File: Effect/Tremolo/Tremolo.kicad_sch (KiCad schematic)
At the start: 28 parts, among them J1 Conn_01x04_Pin, J2 Conn_01x03_Pin, Q1 MBT2222ADW1T1, Q2 MMBF5103, Q3 BC846

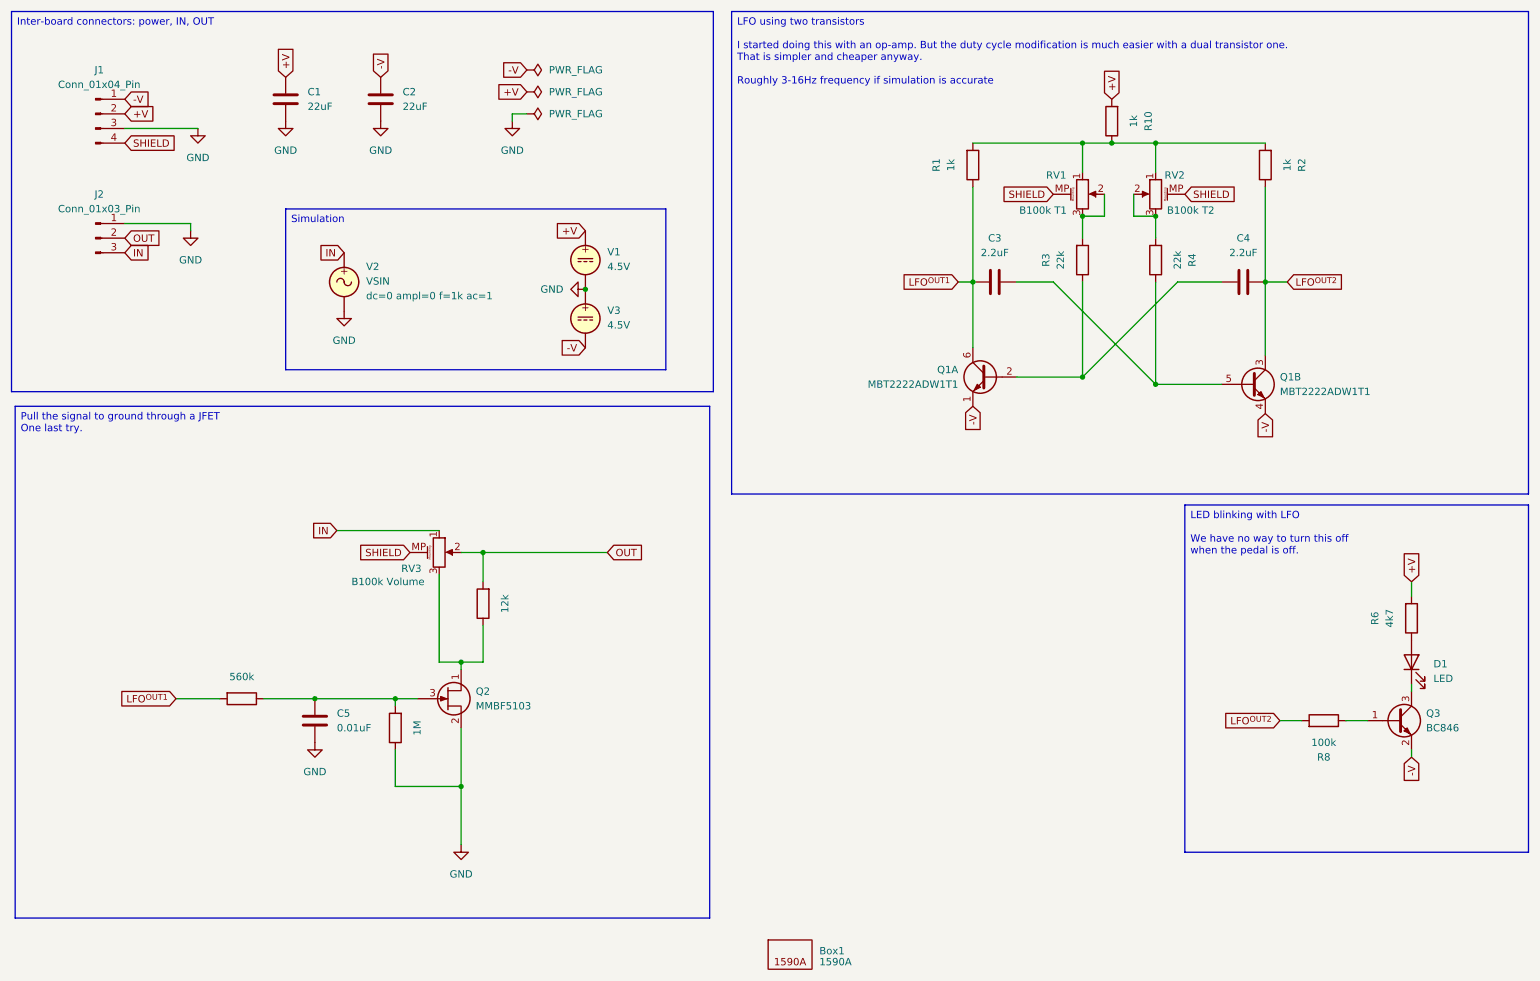
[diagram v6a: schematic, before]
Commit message: Start converting effects boards to the 5V base board: tremolo
The original effects boards were designed to not actually care too much
about the details of the voltage rail, but that was never true of the
tremolo board - because the transistor V_{GS(off)} voltage matters.

Yet the tremolo board was made to _look_ like it didn't care about the
details of the rails, having the non-specific +V and -V rails, and
calling the signal ground reference "GND".

That signal ground vs power ground thing obviously then caused the
additional issue with the schematic using the signal voltage reference
as a power rail for the LFO, fixed in commit 63201d9 ("Quick dirty fix
for tremolo board").

The digital effects boards already made their voltage rails explicit,
and match the base board they require.  Let's just start doing that with
the other effects boards too, starting with the tremolo that cares the
most.

Since I have to start using the 5V rail-to-rail op amps anyway, and I
don't want to have lots of component variations for different boards, I
think I'm going to convert them all to the new world order.

And while 9V may be traditional, a lot of modern components seem to all
be geared to 5V or less.  Of course, there are also op amps like the
OPAx991 family that have very wide voltage rails indeed, and are RtR
from 2.7V to 40V rails.  But with other components having much more
limited voltage ranges, I don't think it's worth designing different
base boards.

For the tremolo board, the only real change for 5V involves removing the
voltage divider resistor that was part of driving the JFET.  With the 9V
voltage rails, that just intentionally limited the gate voltage swing.

Now, with the 5V rails, it ended up limiting the gate voltage too much,
and the JFET might not turn on at all depending on exactly where
V_{GS(off)} ends up being.

And since we're now being honest about what is real ground, just make
the shield be GND and use a full ground pour.

Signed-off-by: Linus Torvalds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
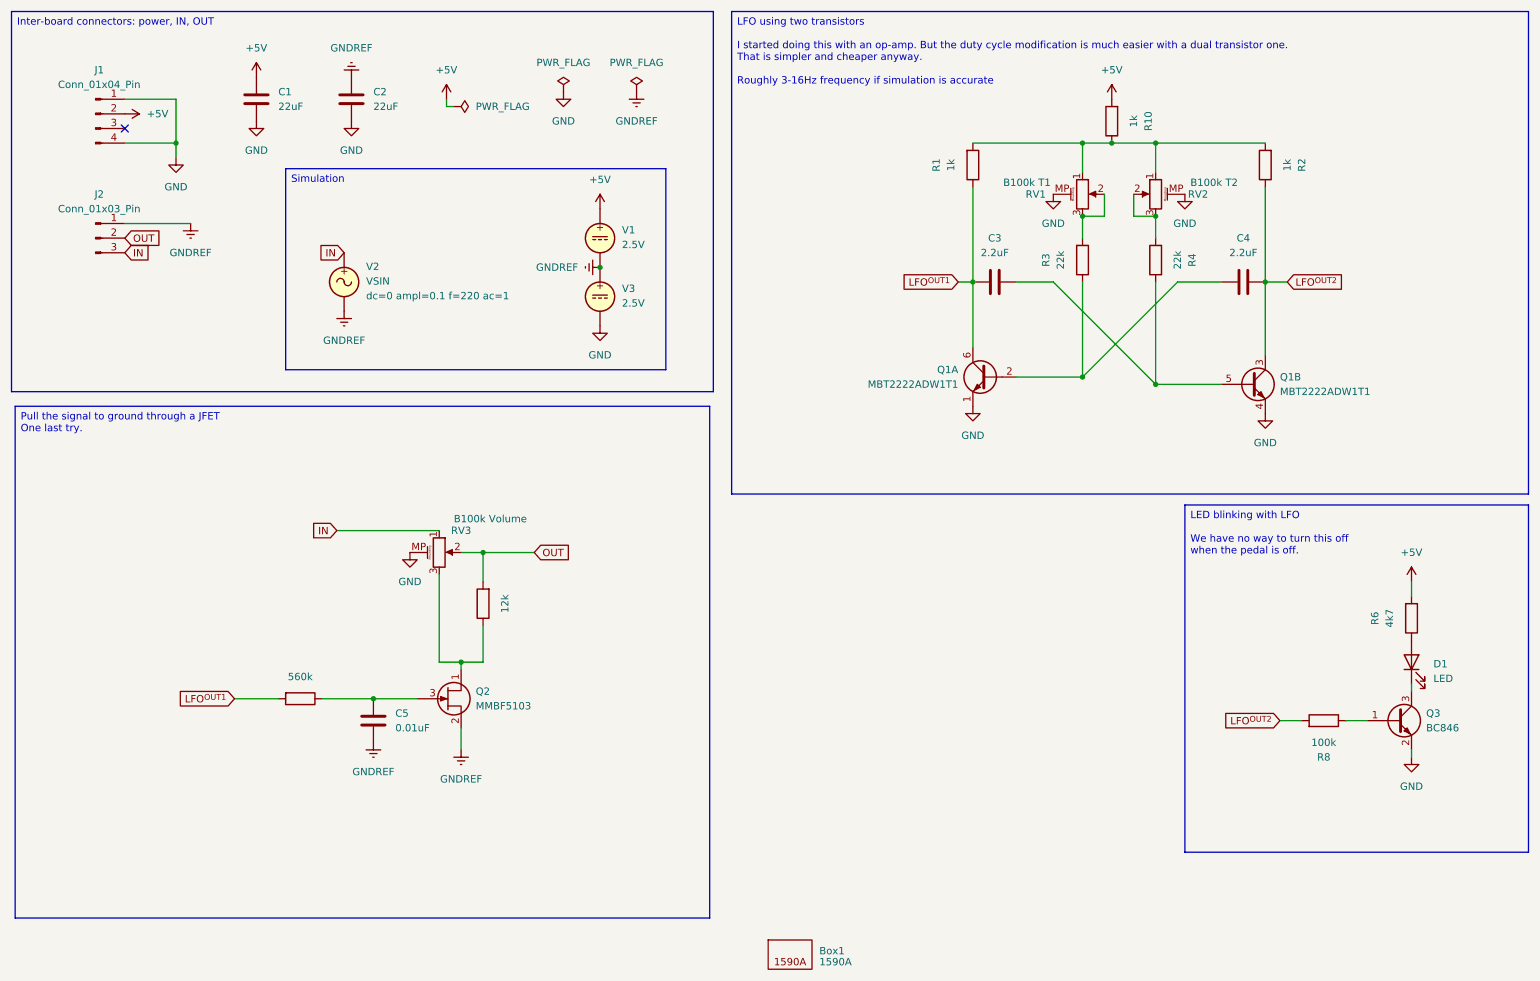
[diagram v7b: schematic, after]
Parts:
- removed R9: 1M, Resistor_SMD:R_0805_2012Metric_Pad1.20x1.40mm_HandSolder, symbol Device:R
- V1, V3: value 4.5V -> 2.5V
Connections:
- net SHIELD is gone; now on net GND: J1.4 (Pin_4), RV1.MP (MountPin), RV2.MP (MountPin), RV3.MP (MountPin)
- net GND: now also J1.1 (Pin_1), Q1.1 (E1), Q1.4 (E2), Q3.2 (E), V3.2; no longer C5.1, J1.3 (Pin_3), J2.1 (Pin_1), Q2.2 (S), V1.2, V2.2, V3.1
- net +V renamed +5V
- removed net -V: C2.1, J1.1 (Pin_1), Q1.1 (E1), Q1.4 (E2), Q3.2 (E), V3.2
- new net GNDREF: C2.1, C5.1, J2.1 (Pin_1), Q2.2 (S), V1.2, V2.2, V3.1
- no-connect marks 0 -> 1
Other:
- moved on the sheet: C1, C2, C5, V1, V3

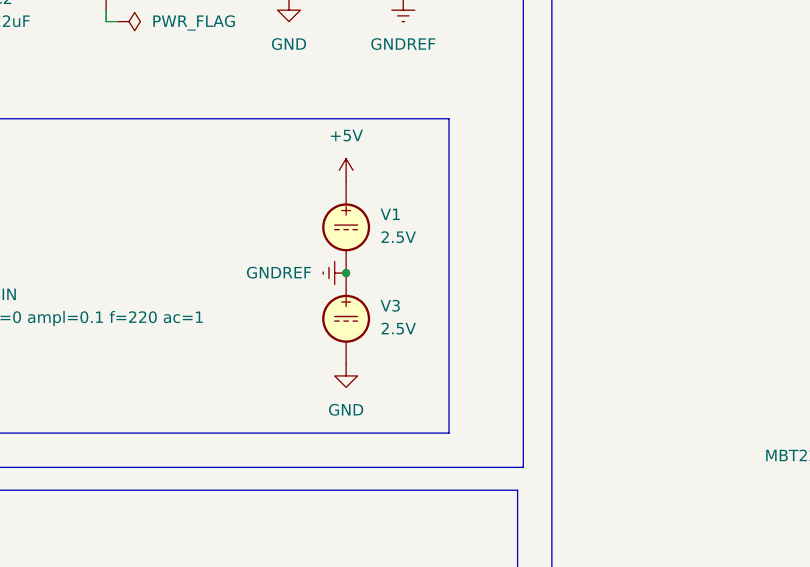
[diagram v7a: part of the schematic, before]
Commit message: Update all remaining effects boards to use global ground and GNDREF
Let's just make it the rule that we only call the actual external ground
GND, and don't play with local grounds.  That makes things like the
potentiometer shield pins so much simpler to deal with, and means that
ground pours are actual ground pours.

The GNDREF uses are fairly few in the end, and it's much better to make
them explicit.

Signed-off-by: Linus Torvalds <torvalds@linux-foundation.org>
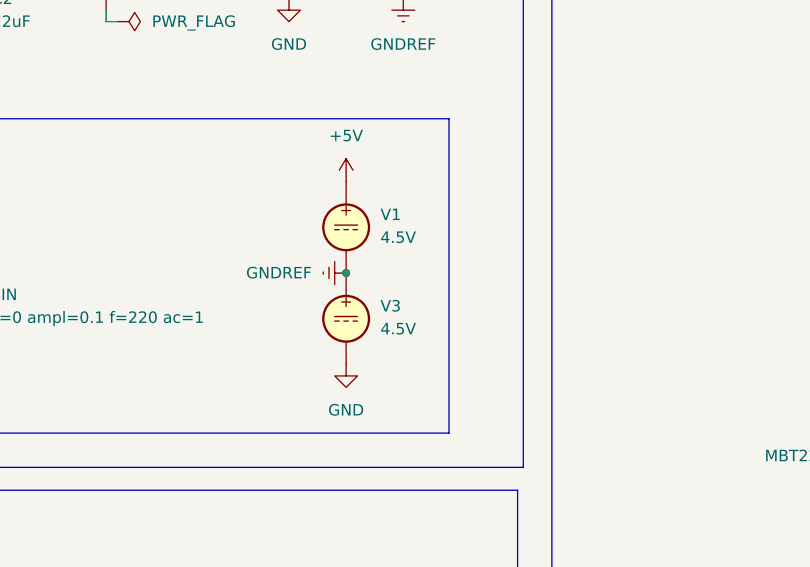
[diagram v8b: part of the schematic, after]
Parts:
- V1, V3: value 2.5V -> 4.5V
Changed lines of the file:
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@@
 			)
 		)
-		(property "Value" "2.5V"
+		(property "Value" "4.5V"
 			(at 120.65 65.9101 0)
 			(effects
@@
 			)
 		)
-		(property "Value" "2.5V"
+		(property "Value" "4.5V"
 			(at 120.65 55.7501 0)
 			(effects
